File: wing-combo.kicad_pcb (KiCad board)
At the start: 2 copper layers, 93 x 91.3 mm, 114 parts, among them J1 Screw_Terminal_01x06, J13 USB_A, J15 Conn_01x16, J16 Conn_01x16, J17 Screw_Terminal_01x06, J18 Screw_Terminal_01x06, J3 Conn_01x12, J4 Conn_01x12, T1 AO3400A, T2 AO3400A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

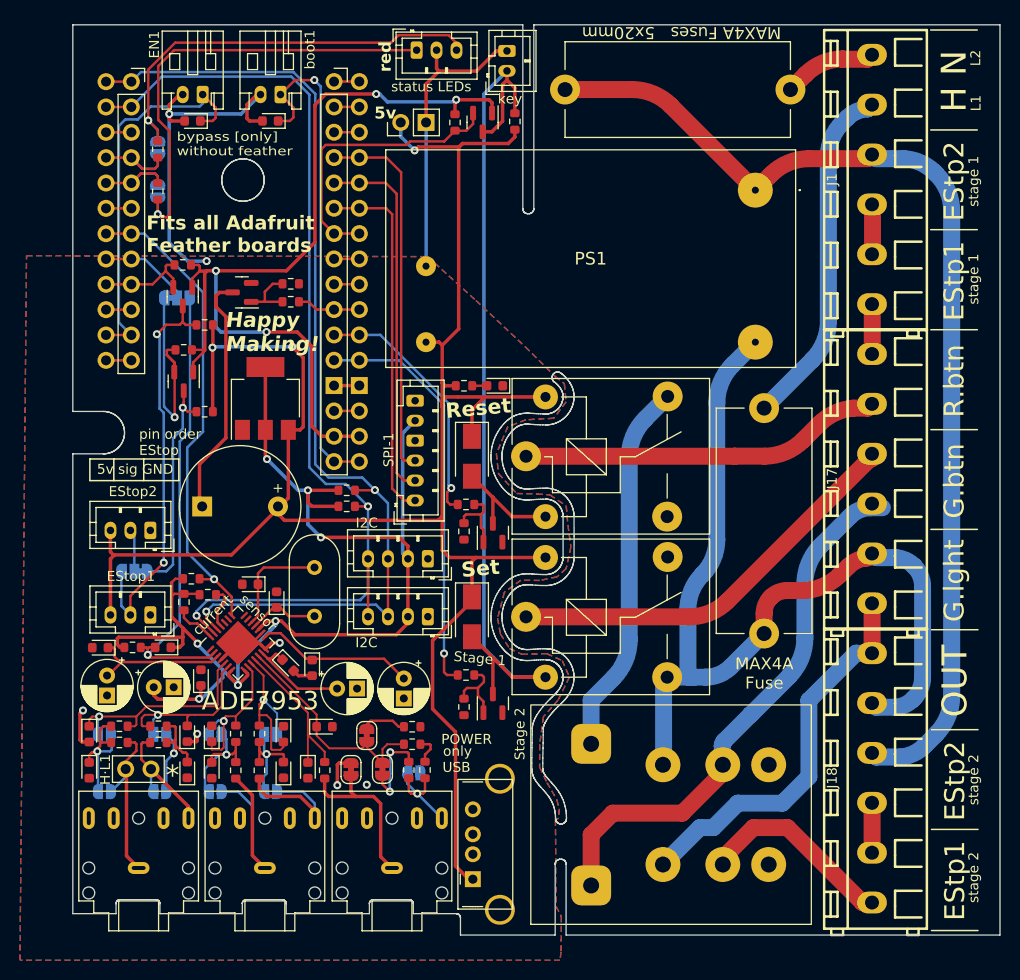
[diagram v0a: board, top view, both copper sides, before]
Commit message: [fix] bypass key and high-voltage routing
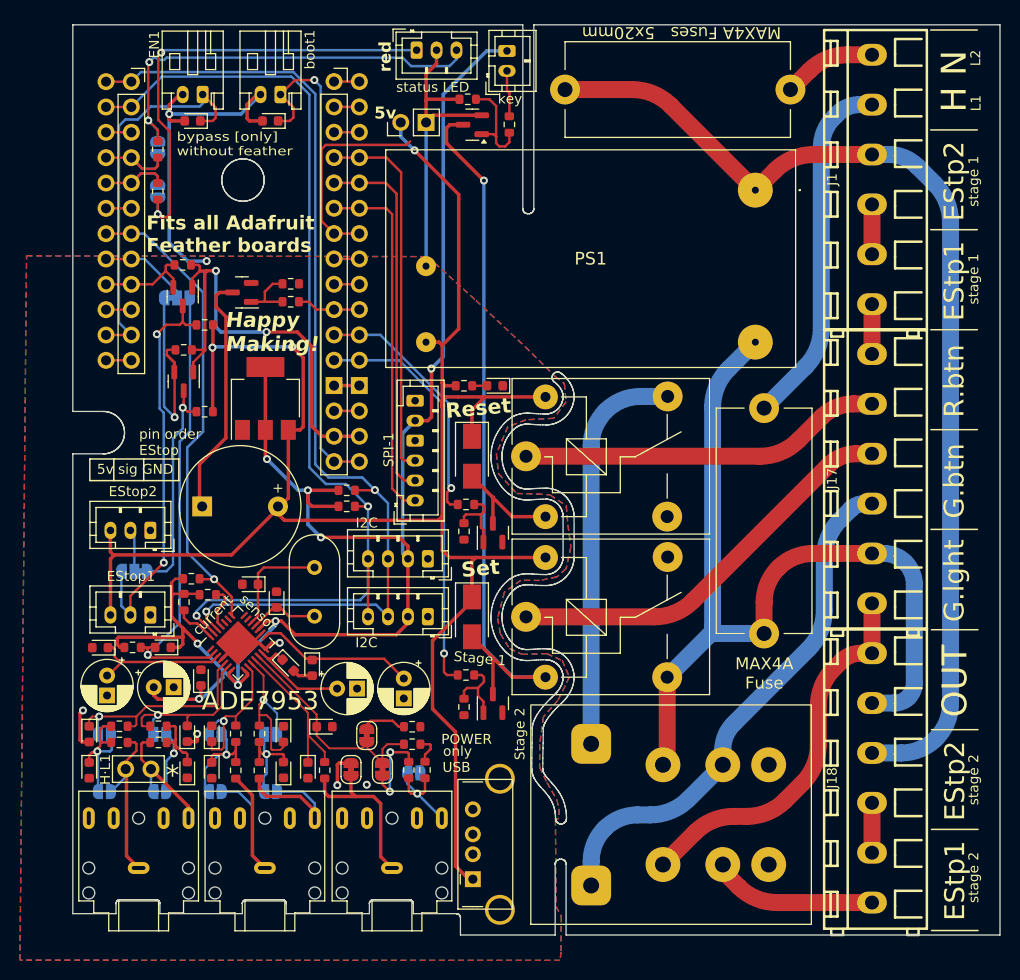
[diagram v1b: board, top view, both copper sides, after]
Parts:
- removed R32, R33: 10k, Resistor_SMD:R_0603_1608Metric
- removed T5: AO3400A, Package_TO_SOT_SMD:SOT-23
- added R36: 1k, Resistor_SMD:R_0603_1608Metric, F.Cu at (80.7, 32.9)
- added R37: 10k, Resistor_SMD:R_0603_1608Metric, F.Cu at (76.5, 30.4)
- added T7: AO3400A, Package_TO_SOT_SMD:SOT-23, F.Cu at (77.0, 32.9)
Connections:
- net 3vRead-Bypass renamed Read-Bypass
- Bypass-1 pad 2: GND -> +3.3V
- D3 pad 2: read-bypass -> Net-(D3-A)
- T3 pad 3: read-bypass -> Net-(D3-A)
- relay1 pad 2: read-bypass -> Net-(D3-A)
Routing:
- net read-bypass: track 90.2 -> 4.64 mm
- net Net-(D3-A): track 0.00 -> 75.5 mm, vias 0 -> 1
- net +3.3VA: track 92.4 -> 46.2 mm, vias 4 -> 2
- net +3.3V: track 126.7 -> 169.6 mm, vias 7 -> 8
- net +5V: track 201.7 -> 191.3 mm
- net Net-(T7-G): track 0.00 -> 10.2 mm
- net Read-Bypass: track 28.9 -> 20.7 mm
- net Green-Indicator-light-1: track 94.7 -> 89.7 mm
- net Member-E-Stop-sw1-1: track 20.0 -> 16.6 mm
- net reset: track 37.5 -> 40.3 mm
- net Member-Green-Button-2: track 54.9 -> 52.7 mm
- net GND: track 91.1 -> 93.2 mm
- net Member-E-Stop-aux2-2: track 107.3 -> 106.4 mm
- net Net-(JP15-B): track 43.4 -> 44.2 mm, vias 1 -> 2
- net H/L1: track 34.9 -> 35.8 mm
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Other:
- board text added: "status LED"
- board text removed: "status LEDs"

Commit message: [fix] read-bypass link
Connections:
- J15 pad 7: Read-Bypass -> read-bypass
- J16 pad 7: Read-Bypass -> read-bypass
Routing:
- net read-bypass: track 4.64 -> 41.3 mm, vias 0 -> 2
- net Read-Bypass: track 20.7 -> 0.00 mm
- net +5V: vias 3 -> 2
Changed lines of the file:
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@@
 	(net 94 "unconnected-(SPI-1-Pin_4-Pad4)")
 	(net 95 "Net-(D3-A)")
-	(net 96 "Read-Bypass")
-	(net 97 "Net-(T7-G)")
+	(net 96 "Net-(T7-G)")
 	(footprint "Connector_JST:JST_PH_B3B-PH-K_1x03_P2.00mm_Vertical"
 		(layer "F.Cu")
@@
 			(layers "F.Cu" "F.Paste" "F.Mask")
 			(roundrect_rratio 0.25)
-			(net 97 "Net-(T7-G)")
+			(net 96 "Net-(T7-G)")
 			(pintype "passive")
 		)
@@
 			(layers "*.Cu" "*.Mask")
 			(remove_unused_layers no)
-			(net 96 "Read-Bypass")
+			(net 2 "read-bypass")
 			(pinfunction "Pin_7")
 			(pintype "passive")
@@
 			(layers "F.Cu" "F.Paste" "F.Mask")
 			(roundrect_rratio 0.25)
-			(net 97 "Net-(T7-G)")
+			(net 96 "Net-(T7-G)")
 			(pinfunction "G")
 			(pintype "input")
@@
 			(layers "F.Cu" "F.Paste" "F.Mask")
 			(roundrect_rratio 0.25)
-			(net 97 "Net-(T7-G)")
+			(net 96 "Net-(T7-G)")
 			(pintype "passive")
 		)
@@
 			(layers "*.Cu" "*.Mask")
 			(remove_unused_layers no)
-			(net 96 "Read-Bypass")
+			(net 2 "read-bypass")
 			(pinfunction "Pin_7")
 			(pintype "passive")
@@
 	)
 	(segment
+		(start 67.275 31.85)
+		(end 67.275 34.025)
+		(width 0.25)
+		(layer "F.Cu")
+		(net 2)
+	)
+	(segment
+		(start 79.805 27.53)
+		(end 80.435 27.53)
+		(width 0.25)
+		(layer "F.Cu")
+		(net 2)
+	)
+	(segment
+		(start 67.275 34.025)
+		(end 66.325 34.975)
+		(width 0.25)
+		(layer "F.Cu")
+		(net 2)
+	)
+	(segment
+		(start 61.825 42.57)
+		(end 63.095 43.84)
+		(width 0.25)
+		(layer "F.Cu")
+		(net 2)
+	)
+	(segment
 		(start 80.675 29.725)
 		(end 80.435 29.485)
@@
 	)
 	(segment
+		(start 68.3 30.825)
+		(end 67.275 31.85)
+		(width 0.25)
+		(layer "F.Cu")
+		(net 2)
+	)
+	(segment
+		(start 70.975 30.825)
+		(end 68.3 30.825)
+		(width 0.25)
+		(layer "F.Cu")
+		(net 2)
+	)
+	(segment
+		(start 61.825 35.395)
+		(end 61.825 42.57)
+		(width 0.25)
+		(layer "F.Cu")
+		(net 2)
+	)
+	(segment
+		(start 66.325 34.975)
+		(end 62.245 34.975)
+		(width 0.25)
+		(layer "F.Cu")
+		(net 2)
+	)
+	(segment
+		(start 62.245 34.975)
+		(end 61.825 35.395)
+		(width 0.25)
+		(layer "F.Cu")
+		(net 2)
+	)
+	(segment
+		(start 77.475 25.2)
+		(end 79.805 27.53)
+		(width 0.25)
+		(layer "F.Cu")
+		(net 2)
+	)
+	(segment
+		(start 65.635 43.84)
+		(end 63.095 43.84)
+		(width 0.25)
+		(layer "F.Cu")
+		(net 2)
+	)
+	(segment
 		(start 80.435 29.485)
 		(end 80.435 27.53)
@@
 		(net 2)
 	)
+	(via
+		(at 77.475 25.2)
+		(size 0.8)
+		(drill 0.4)
+		(layers "F.Cu" "B.Cu")
+		(net 2)
+	)
+	(via
+		(at 70.975 30.825)
+		(size 0.8)
+		(drill 0.4)
+		(layers "F.Cu" "B.Cu")
+		(net 2)
+	)
+	(segment
+		(start 72 30.825)
+		(end 70.975 30.825)
+		(width 0.25)
+		(layer "B.Cu")
+		(net 2)
+	)
+	(segment
+		(start 77.475 25.35)
+		(end 72 30.825)
+		(width 0.25)
+		(layer "B.Cu")
+		(net 2)
+	)
+	(segment
+		(start 77.475 25.2)
+		(end 77.475 25.35)
+		(width 0.25)
+		(layer "B.Cu")
+		(net 2)
+	)
+	(segment
+		(start 75.595 39.92)
+		(end 69.785 34.11)
+		(width 0.35)
+		(layer "F.Cu")
+		(net 3)
+	)
 	(segment
 		(start 76.925 80.7)
@@
 	)
 	(segment
+		(start 69.785 34.11)
+		(end 69.785 32.7)
+		(width 0.35)
+		(layer "F.Cu")
+		(net 3)
+	)
+	(segment
 		(start 60.255 72.59)
 		(end 58.125 72.59)
@@
 	)
 	(segment
-		(start 50.905 55.27)
-		(end 50.95 55.225)
+		(start 75.595 53.394)
+		(end 75.595 39.92)
 		(width 0.35)
 		(layer "F.Cu")
@@
 	)
 	(segment
-		(start 40.68 76.465)
-		(end 40.68 82.08)
+		(start 50.905 55.27)
+		(end 50.95 55.225)
 		(width 0.35)
 		(layer "F.Cu")
@@
 	)
 	(segment
-		(start 73.9437 55.0453)
-		(end 75.595 53.394)
+		(start 40.68 76.465)
+		(end 40.68 82.08)
 		(width 0.35)
 		(layer "F.Cu")
@@
 	)
 	(segment
+		(start 73.9437 55.0453)
+		(end 75.595 53.394)
+		(width 0.35)
+		(layer "F.Cu")
+		(net 3)
+	)
+	(segment
 		(start 72.975 84.65)
 		(end 76.925 80.7)
@@
 	)
 	(segment
-		(start 75.595 53.394)
-		(end 75.595 40.375)
-		(width 0.35)
-		(layer "F.Cu")
-		(net 3)
-	)
-	(segment
 		(start 84.2966 60.2198)
 		(end 78.225 60.2198)
@@
 	)
 	(segment
-		(start 75.595 39.92)
-		(end 71.175 35.5)
-		(width 0.35)
-		(layer "F.Cu")
-		(net 3)
-	)
-	(segment
 		(start 76.925 76.7176)
 		(end 77.325 76.3176)
@@
 	)
 	(segment
-		(start 75.595 40.375)
-		(end 75.595 39.92)
-		(width 0.35)
-		(layer "F.Cu")
-		(net 3)
-	)
-	(segment
 		(start 58.905 55.18)
 		(end 60.005 56.28)
@@
 	)
 	(via
-		(at 71.175 35.5)
-		(size 0.8)
-		(drill 0.4)
-		(layers "F.Cu" "B.Cu")
-		(net 3)
-	)
-	(via
 		(at 50.905 55.27)
 		(size 0.8)
@@
 	)
 	(segment
-		(start 71.175 35.5)
-		(end 69.785 34.11)
-		(width 0.35)
-		(layer "B.Cu")
-		(net 3)
-	)
-	(segment
 		(start 58.895 55.19)
 		(end 50.985 55.19)
@@
 	)
 	(segment
-		(start 69.785 34.11)
-		(end 69.785 32.7)
-		(width 0.35)
-		(layer "B.Cu")
-		(net 3)
-	)
-	(segment
 		(start 107.314407 37.508792)
 		(end 105.3366 39.4866)
@@
 	)
 	(segment
-		(start 61.825 42.57)
-		(end 61.825 35.395)
-		(width 0.25)
-		(layer "F.Cu")
-		(net 96)
-	)
-	(segment
-		(start 70.375 34.95)
-		(end 70.725 34.6)
-		(width 0.25)
-		(layer "F.Cu")
-		(net 96)
-	)
-	(segment
-		(start 62.27 34.95)
-		(end 70.375 34.95)
-		(width 0.25)
-		(layer "F.Cu")
-		(net 96)
-	)
-	(segment
-		(start 65.635 43.84)
-		(end 63.095 43.84)
-		(width 0.25)
-		(layer "F.Cu")
-		(net 96)
-	)
-	(segment
-		(start 63.095 43.84)
-		(end 61.825 42.57)
-		(width 0.25)
-		(layer "F.Cu")
-		(net 96)
-	)
-	(segment
-		(start 61.825 35.395)
-		(end 62.27 34.95)
-		(width 0.25)
-		(layer "F.Cu")
-		(net 96)
-	)
-	(segment
 		(start 78.675 30.375)
 		(end 79.35 31.05)
 		(width 0.25)
 		(layer "F.Cu")
-		(net 97)
+		(net 96)
 	)
 	(segment
@@
 		(width 0.25)
 		(layer "F.Cu")
-		(net 97)
+		(net 96)
 	)
 	(segment
@@
 		(width 0.25)
 		(layer "F.Cu")
-		(net 97)
+		(net 96)
 	)
 	(segment
@@
 		(width 0.25)
 		(layer "F.Cu")
-		(net 97)
+		(net 96)
 	)
 	(segment
@@
 		(width 0.25)
 		(layer "F.Cu")
-		(net 97)
+		(net 96)
 	)
 	(segment
@@
 		(width 0.25)
 		(layer "F.Cu")
-		(net 97)
+		(net 96)
 	)
 	(segment
@@
 		(width 0.25)
 		(layer "F.Cu")
-		(net 97)
+		(net 96)
 	)
 	(segment
@@
 		(width 0.25)
 		(layer "F.Cu")
-		(net 97)
+		(net 96)
 	)
 	(segment
@@
 		(width 0.25)
 		(layer "F.Cu")
-		(net 97)
+		(net 96)
 	)
 	(segment
@@
 		(width 0.25)
 		(layer "F.Cu")
-		(net 97)
+		(net 96)
 	)
 	(zone

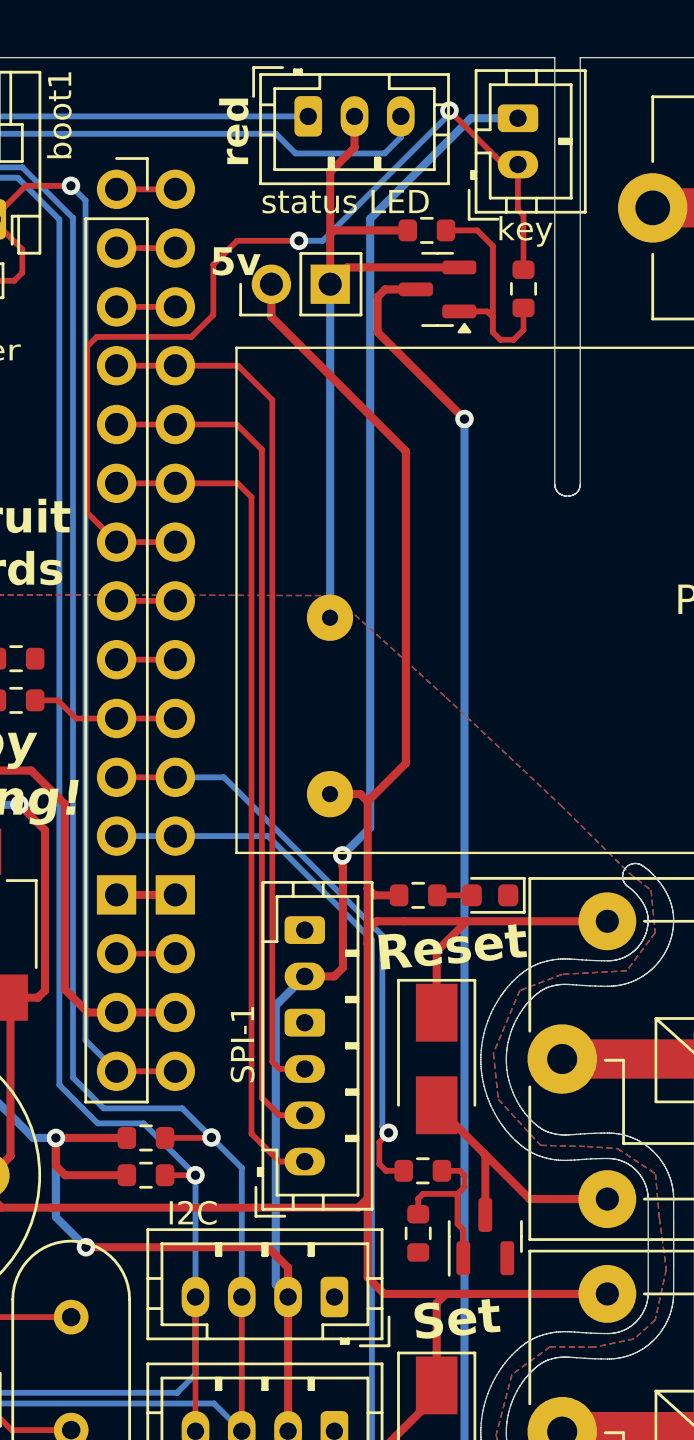
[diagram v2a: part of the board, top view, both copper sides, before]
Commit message: [new] assigned CS pin for JST-SPI and Ethernet Feather-Wing
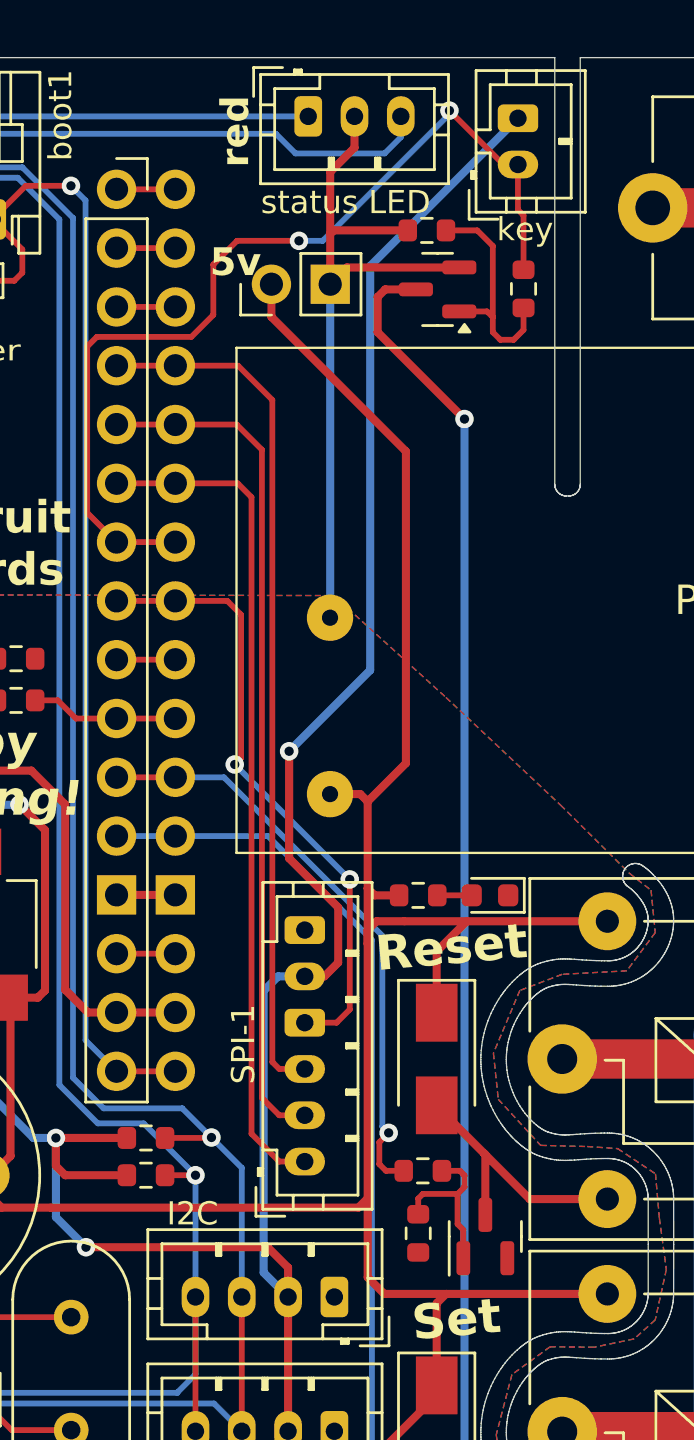
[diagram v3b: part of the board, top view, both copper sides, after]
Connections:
- net Net-(J3-Pin_6) renamed CS-eth0
- J15 pad 8: Net-(J15-Pin_8) -> CS-jst
- J16 pad 8: Net-(J15-Pin_8) -> CS-jst
- SPI-1 pad 4: unconnected-(SPI-1-Pin_4-Pad4) -> CS-jst
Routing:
- net CS-jst: track 0.00 -> 27.0 mm, vias 0 -> 2
- net Net-(J15-Pin_8): track 2.54 -> 0.00 mm
- net +3.3V: track 169.6 -> 171.0 mm
